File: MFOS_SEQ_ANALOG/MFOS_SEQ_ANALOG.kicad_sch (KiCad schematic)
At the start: 94 parts, among them J1 Conn_01x01, J10 Conn_01x01, J2 Conn_01x01, J3 Conn_01x01, J4 Conn_01x01, J5 Conn_01x01, J6 Conn_01x01, J7 Conn_01x01, J8 Conn_01x01, J9 Conn_01x01, U1 TL084, U2 4067, U3 TL082

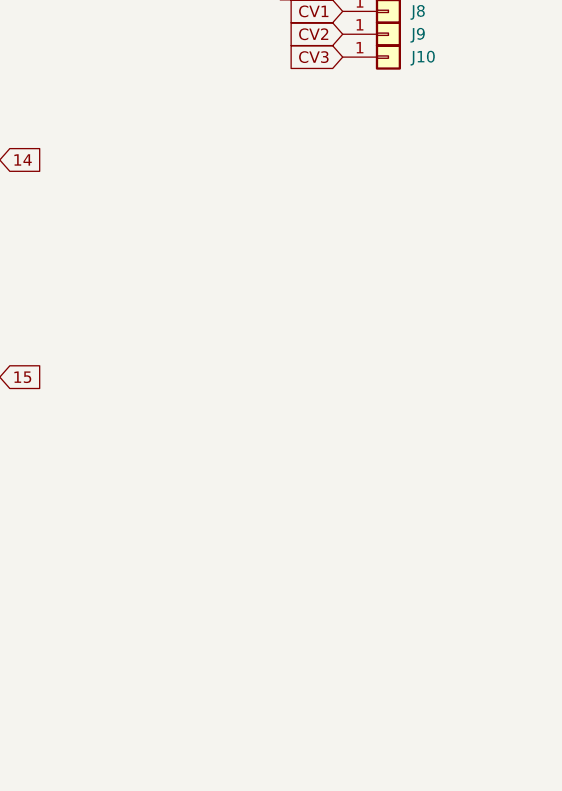
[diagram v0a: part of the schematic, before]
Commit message: Updated BOM, renamed VCO > MFOS_VCO
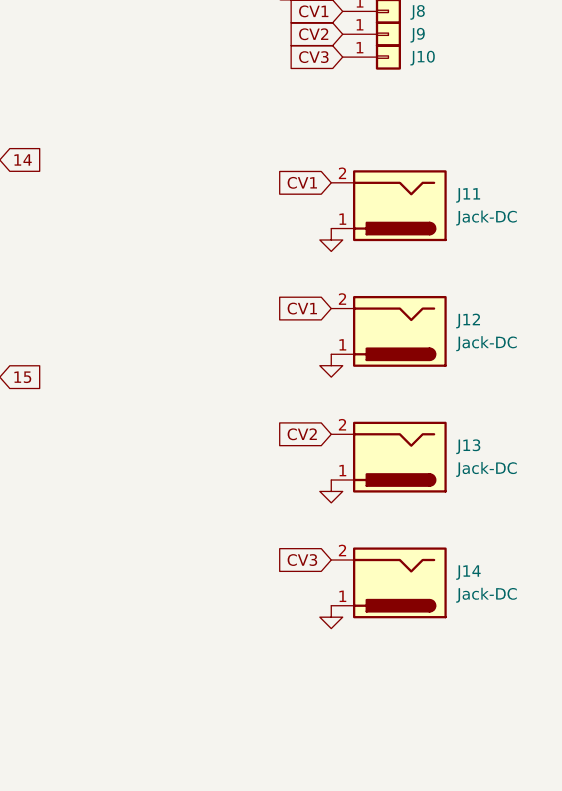
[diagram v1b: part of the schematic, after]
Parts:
- added J11, J12, J13, J14: Jack-DC, symbol Connector:Jack-DC
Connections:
- net CV1: now also J11.2, J12.2
- net CV2: now also J13.2
- net CV3: now also J14.2
- net GND: now also J11.1, J12.1, J13.1, J14.1
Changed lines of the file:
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@@
+    )
+  )
+  (global_label "CV2" (shape input) (at 233.68 102.87 180) (fields_autoplaced)
+    (effects (font (size 1.27 1.27)) (justify right))
+    (property "Intersheet References" "${INTERSHEET_REFS}" (id 0) (at 227.6988 102.7906 0)
+      (effects (font (size 1.27 1.27)) (justify right) hide)
     )
   )
@@
     )
   )
+  (global_label "CV3" (shape input) (at 233.68 116.84 180) (fields_autoplaced)
+    (effects (font (size 1.27 1.27)) (justify right))
+    (property "Intersheet References" "${INTERSHEET_REFS}" (id 0) (at 227.6988 116.7606 0)
+      (effects (font (size 1.27 1.27)) (justify right) hide)
+    )
+  )
   (global_label "8" (shape input) (at 60.96 102.87 0) (fields_autoplaced)
     (effects (font (size 1.27 1.27)) (justify left))
@@
     )
   )
+  (global_label "CV1" (shape input) (at 233.68 88.9 180) (fields_autoplaced)
+    (effects (font (size 1.27 1.27)) (justify right))
+    (property "Intersheet References" "${INTERSHEET_REFS}" (id 0) (at 227.6988 88.8206 0)
+      (effects (font (size 1.27 1.27)) (justify right) hide)
+    )
+  )
   (global_label "6" (shape input) (at 60.96 97.79 0) (fields_autoplaced)
     (effects (font (size 1.27 1.27)) (justify left))
@@
     )
   )
+  (global_label "CV1" (shape input) (at 233.68 74.93 180) (fields_autoplaced)
+    (effects (font (size 1.27 1.27)) (justify right))
+    (property "Intersheet References" "${INTERSHEET_REFS}" (id 0) (at 227.6988 74.8506 0)
+      (effects (font (size 1.27 1.27)) (justify right) hide)
+    )
+  )
   (symbol (lib_id "Device:R") (at 160.02 106.68 90) (unit 1)
     (in_bom yes) (on_board yes)
@@
     )
     (property "Datasheet" "~" (id 3) (at 189.23 96.52 0)
+      (effects (font (size 1.27 1.27)) hide)
+    )
+    (pin "1")
+    (pin "2")
+  )
+  (symbol (lib_id "Connector:Jack-DC") (at 241.3 77.47 180) (unit 1)
+    (in_bom yes) (on_board yes) (fields_autoplaced)
+    (property "Reference" "J11" (id 0) (at 247.65 76.1999 0)
+      (effects (font (size 1.27 1.27)) (justify right))
+    )
+    (property "Value" "Jack-DC" (id 1) (at 247.65 78.7399 0)
+      (effects (font (size 1.27 1.27)) (justify right))
+    )
+    (property "Footprint" "" (id 2) (at 240.03 76.454 0)
+      (effects (font (size 1.27 1.27)) hide)
+    )
+    (property "Datasheet" "~" (id 3) (at 240.03 76.454 0)
       (effects (font (size 1.27 1.27)) hide)
     )
@@
     (pin "3")
   )
+  (symbol (lib_id "power:GND") (at 233.68 107.95 0) (unit 1)
+    (in_bom yes) (on_board yes) (fields_autoplaced)
+    (property "Reference" "#PWR033" (id 0) (at 233.68 114.3 0)
+      (effects (font (size 1.27 1.27)) hide)
+    )
+    (property "Value" "GND" (id 1) (at 233.68 113.03 0)
+      (effects (font (size 1.27 1.27)) hide)
+    )
+    (property "Footprint" "" (id 2) (at 233.68 107.95 0)
+      (effects (font (size 1.27 1.27)) hide)
+    )
+    (property "Datasheet" "" (id 3) (at 233.68 107.95 0)
+      (effects (font (size 1.27 1.27)) hide)
+    )
+    (pin "1")
+  )
   (symbol (lib_id "power:GND") (at 72.39 153.67 0) (unit 1)
     (in_bom yes) (on_board yes)
@@
     )
     (property "Datasheet" "" (id 3) (at 152.4 63.5 0)
+      (effects (font (size 1.27 1.27)) hide)
+    )
+    (pin "1")
+  )
+  (symbol (lib_id "Connector:Jack-DC") (at 241.3 119.38 180) (unit 1)
+    (in_bom yes) (on_board yes) (fields_autoplaced)
+    (property "Reference" "J14" (id 0) (at 247.65 118.1099 0)
+      (effects (font (size 1.27 1.27)) (justify right))
+    )
+    (property "Value" "Jack-DC" (id 1) (at 247.65 120.6499 0)
+      (effects (font (size 1.27 1.27)) (justify right))
+    )
+    (property "Footprint" "" (id 2) (at 240.03 118.364 0)
+      (effects (font (size 1.27 1.27)) hide)
+    )
+    (property "Datasheet" "~" (id 3) (at 240.03 118.364 0)
+      (effects (font (size 1.27 1.27)) hide)
+    )
+    (pin "1")
+    (pin "2")
+  )
+  (symbol (lib_id "power:GND") (at 233.68 80.01 0) (unit 1)
+    (in_bom yes) (on_board yes) (fields_autoplaced)
+    (property "Reference" "#PWR031" (id 0) (at 233.68 86.36 0)
+      (effects (font (size 1.27 1.27)) hide)
+    )
+    (property "Value" "GND" (id 1) (at 233.68 85.09 0)
+      (effects (font (size 1.27 1.27)) hide)
+    )
+    (property "Footprint" "" (id 2) (at 233.68 80.01 0)
+      (effects (font (size 1.27 1.27)) hide)
+    )
+    (property "Datasheet" "" (id 3) (at 233.68 80.01 0)
       (effects (font (size 1.27 1.27)) hide)
     )
@@
     (pin "1")
   )
+  (symbol (lib_id "Connector:Jack-DC") (at 241.3 91.44 180) (unit 1)
+    (in_bom yes) (on_board yes) (fields_autoplaced)
+    (property "Reference" "J12" (id 0) (at 247.65 90.1699 0)
+      (effects (font (size 1.27 1.27)) (justify right))
+    )
+    (property "Value" "Jack-DC" (id 1) (at 247.65 92.7099 0)
+      (effects (font (size 1.27 1.27)) (justify right))
+    )
+    (property "Footprint" "" (id 2) (at 240.03 90.424 0)
+      (effects (font (size 1.27 1.27)) hide)
+    )
+    (property "Datasheet" "~" (id 3) (at 240.03 90.424 0)
+      (effects (font (size 1.27 1.27)) hide)
+    )
+    (pin "1")
+    (pin "2")
+  )
   (symbol (lib_id "Device:R_Potentiometer") (at 90.17 82.55 0) (unit 1)
     (in_bom yes) (on_board yes)
@@
     (pin "1")
   )
+  (symbol (lib_id "Connector:Jack-DC") (at 241.3 105.41 180) (unit 1)
+    (in_bom yes) (on_board yes) (fields_autoplaced)
+    (property "Reference" "J13" (id 0) (at 247.65 104.1399 0)
+      (effects (font (size 1.27 1.27)) (justify right))
+    )
+    (property "Value" "Jack-DC" (id 1) (at 247.65 106.6799 0)
+      (effects (font (size 1.27 1.27)) (justify right))
+    )
+    (property "Footprint" "" (id 2) (at 240.03 104.394 0)
+      (effects (font (size 1.27 1.27)) hide)
+    )
+    (property "Datasheet" "~" (id 3) (at 240.03 104.394 0)
+      (effects (font (size 1.27 1.27)) hide)
+    )
+    (pin "1")
+    (pin "2")
+  )
   (symbol (lib_id "power:PWR_FLAG") (at 220.98 152.4 0) (unit 1)
     (in_bom yes) (on_board yes) (fields_autoplaced)
@@
     (pin "2")
     (pin "3")
+  )
+  (symbol (lib_id "power:GND") (at 233.68 121.92 0) (unit 1)
+    (in_bom yes) (on_board yes) (fields_autoplaced)
+    (property "Reference" "#PWR034" (id 0) (at 233.68 128.27 0)
+      (effects (font (size 1.27 1.27)) hide)
+    )
+    (property "Value" "GND" (id 1) (at 233.68 127 0)
+      (effects (font (size 1.27 1.27)) hide)
+    )
+    (property "Footprint" "" (id 2) (at 233.68 121.92 0)
+      (effects (font (size 1.27 1.27)) hide)
+    )
+    (property "Datasheet" "" (id 3) (at 233.68 121.92 0)
+      (effects (font (size 1.27 1.27)) hide)
+    )
+    (pin "1")
   )
   (symbol (lib_id "power:+12V") (at 46.99 151.13 0) (unit 1)
@@
     (pin "3")
   )
+  (symbol (lib_id "power:GND") (at 233.68 93.98 0) (unit 1)
+    (in_bom yes) (on_board yes) (fields_autoplaced)
+    (property "Reference" "#PWR032" (id 0) (at 233.68 100.33 0)
+      (effects (font (size 1.27 1.27)) hide)
+    )
+    (property "Value" "GND" (id 1) (at 233.68 99.06 0)
+      (effects (font (size 1.27 1.27)) hide)
+    )
+    (property "Footprint" "" (id 2) (at 233.68 93.98 0)
+      (effects (font (size 1.27 1.27)) hide)
+    )
+    (property "Datasheet" "" (id 3) (at 233.68 93.98 0)
+      (effects (font (size 1.27 1.27)) hide)
+    )
+    (pin "1")
+  )
   (symbol (lib_id "Device:R_Potentiometer") (at 90.17 106.68 0) (unit 1)
     (in_bom yes) (on_board yes)
@@
       (reference "#PWR030") (unit 1) (value "GND") (footprint "")
     )
+    (path "/5e282527-99dc-4429-b4bb-01c140323197"
+      (reference "#PWR031") (unit 1) (value "GND") (footprint "")
+    )
+    (path "/faff02bb-9051-4309-a399-053220f60a01"
+      (reference "#PWR032") (unit 1) (value "GND") (footprint "")
+    )
+    (path "/3fb832e9-263c-4d1e-860f-378e85931e71"
+      (reference "#PWR033") (unit 1) (value "GND") (footprint "")
+    )
+    (path "/d22fdc4c-a9b8-4822-a041-dea36e0169c7"
+      (reference "#PWR034") (unit 1) (value "GND") (footprint "")
+    )
     (path "/0796aec0-e003-4c24-8730-06e74886f345"
       (reference "#PWR0101") (unit 1) (value "GND") (footprint "")
@@
       (reference "J10") (unit 1) (value "Conn_01x01") (footprint "")
     )
+    (path "/16693ef2-3fc4-48c8-8e8f-720027578075"
+      (reference "J11") (unit 1) (value "Jack-DC") (footprint "")
+    )
+    (path "/ae15c61d-fedb-4b67-8420-647c410a8c9e"
+      (reference "J12") (unit 1) (value "Jack-DC") (footprint "")
+    )
+    (path "/c3858c68-019e-47e8-aa21-436341b265be"
+      (reference "J13") (unit 1) (value "Jack-DC") (footprint "")
+    )
+    (path "/5df89b05-9972-48a2-bf2f-54ef2c9d5733"
+      (reference "J14") (unit 1) (value "Jack-DC") (footprint "")
+    )
     (path "/eb2cdd10-f82a-43f7-a1d3-578bfc176dfc"

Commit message: Reviewed BOM
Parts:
- J1, J10, J2, J3, J4, J5, J6, J7, J8, J9: now left out of the parts list

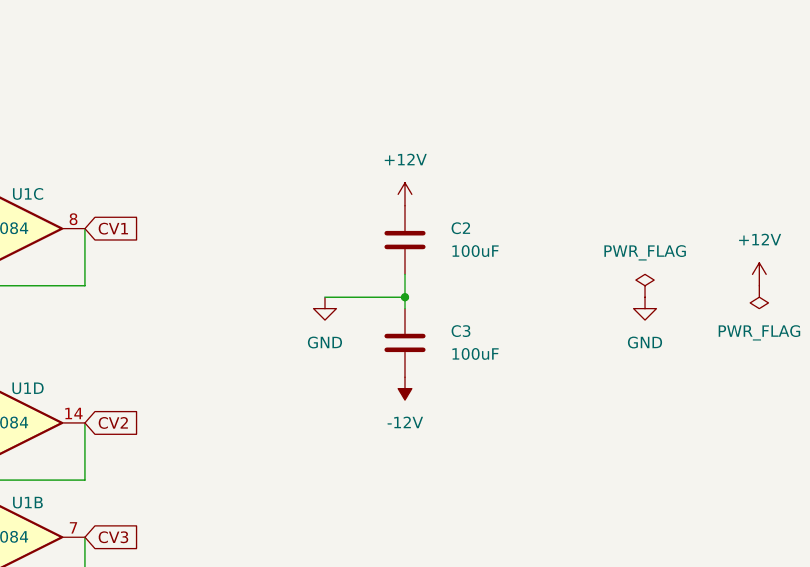
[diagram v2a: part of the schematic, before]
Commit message: Designs adapted for BOM
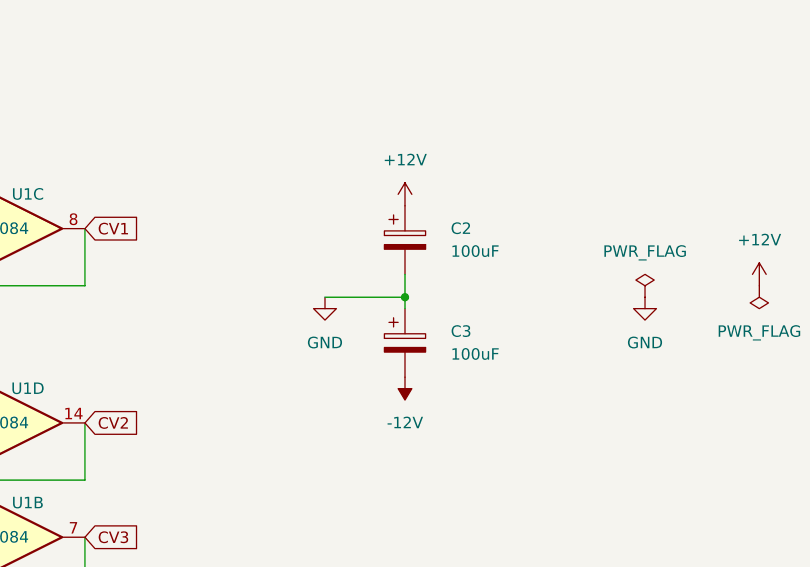
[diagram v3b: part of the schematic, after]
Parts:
- C2, C3: symbol Device:C -> Device:C_Polarized
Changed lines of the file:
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@@
     (pin "9")
   )
-  (symbol (lib_id "Device:C") (at 168.91 157.48 0) (unit 1)
+  (symbol (lib_id "Device:C_Polarized") (at 168.91 157.48 0) (unit 1)
     (in_bom yes) (on_board yes) (fields_autoplaced)
     (property "Reference" "C3" (id 0) (at 173.99 156.2099 0)
@@
     (pin "2")
   )
-  (symbol (lib_id "Device:C") (at 168.91 146.05 0) (unit 1)
+  (symbol (lib_id "Device:C_Polarized") (at 168.91 146.05 0) (unit 1)
     (in_bom yes) (on_board yes) (fields_autoplaced)
     (property "Reference" "C2" (id 0) (at 173.99 144.7799 0)
